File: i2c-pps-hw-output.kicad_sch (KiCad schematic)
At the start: 21 parts, among them J2 Vout, Q7 MMBT3904

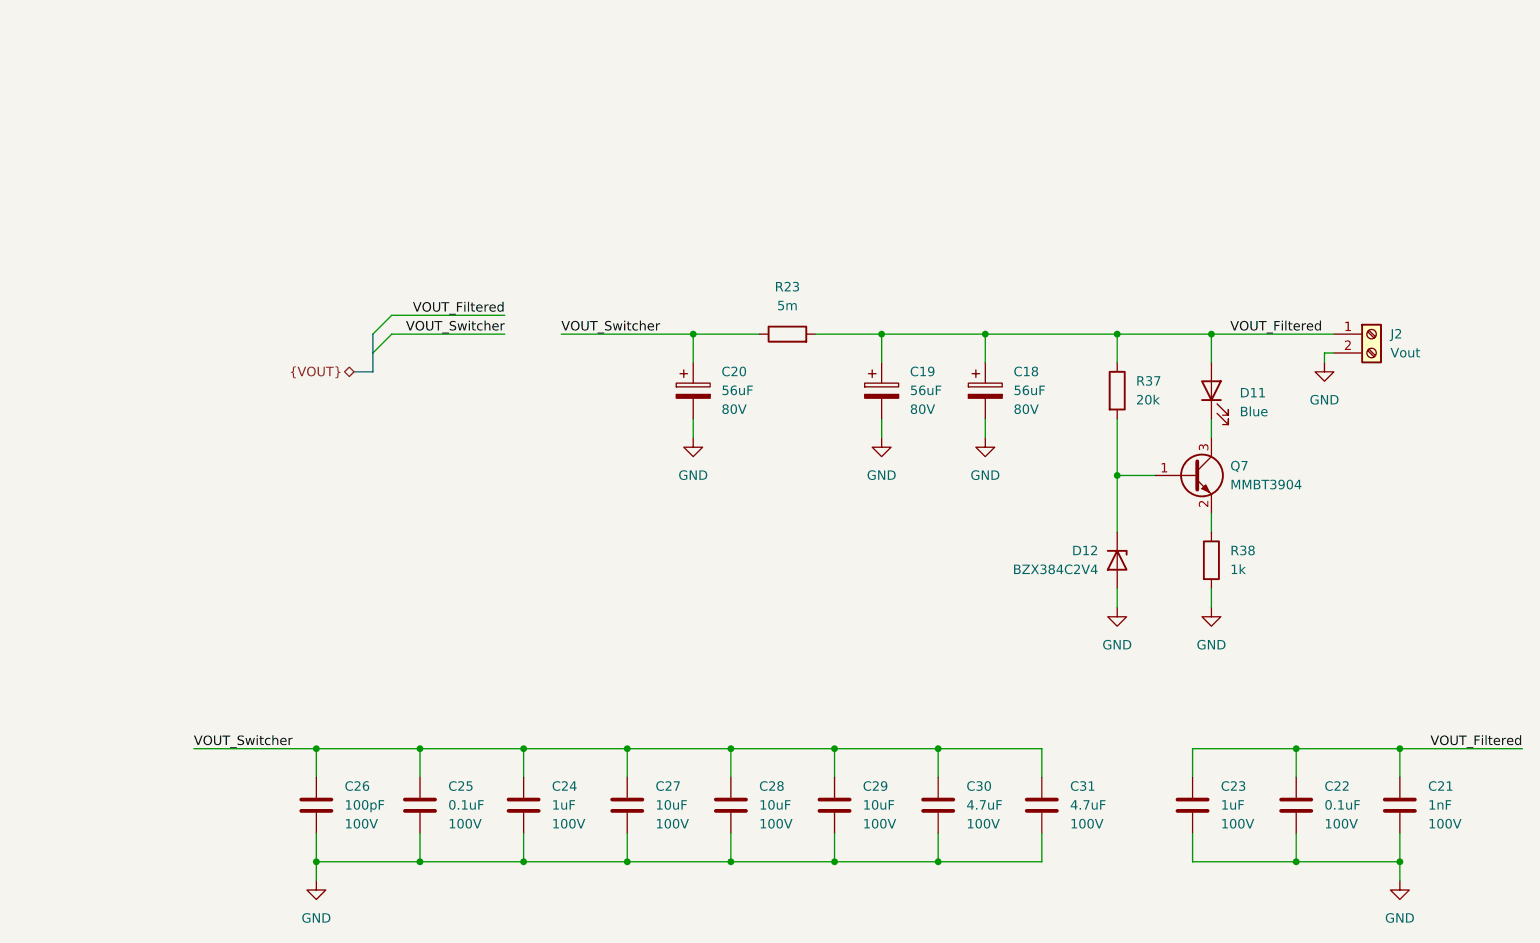
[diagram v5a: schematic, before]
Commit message: Route the PCB
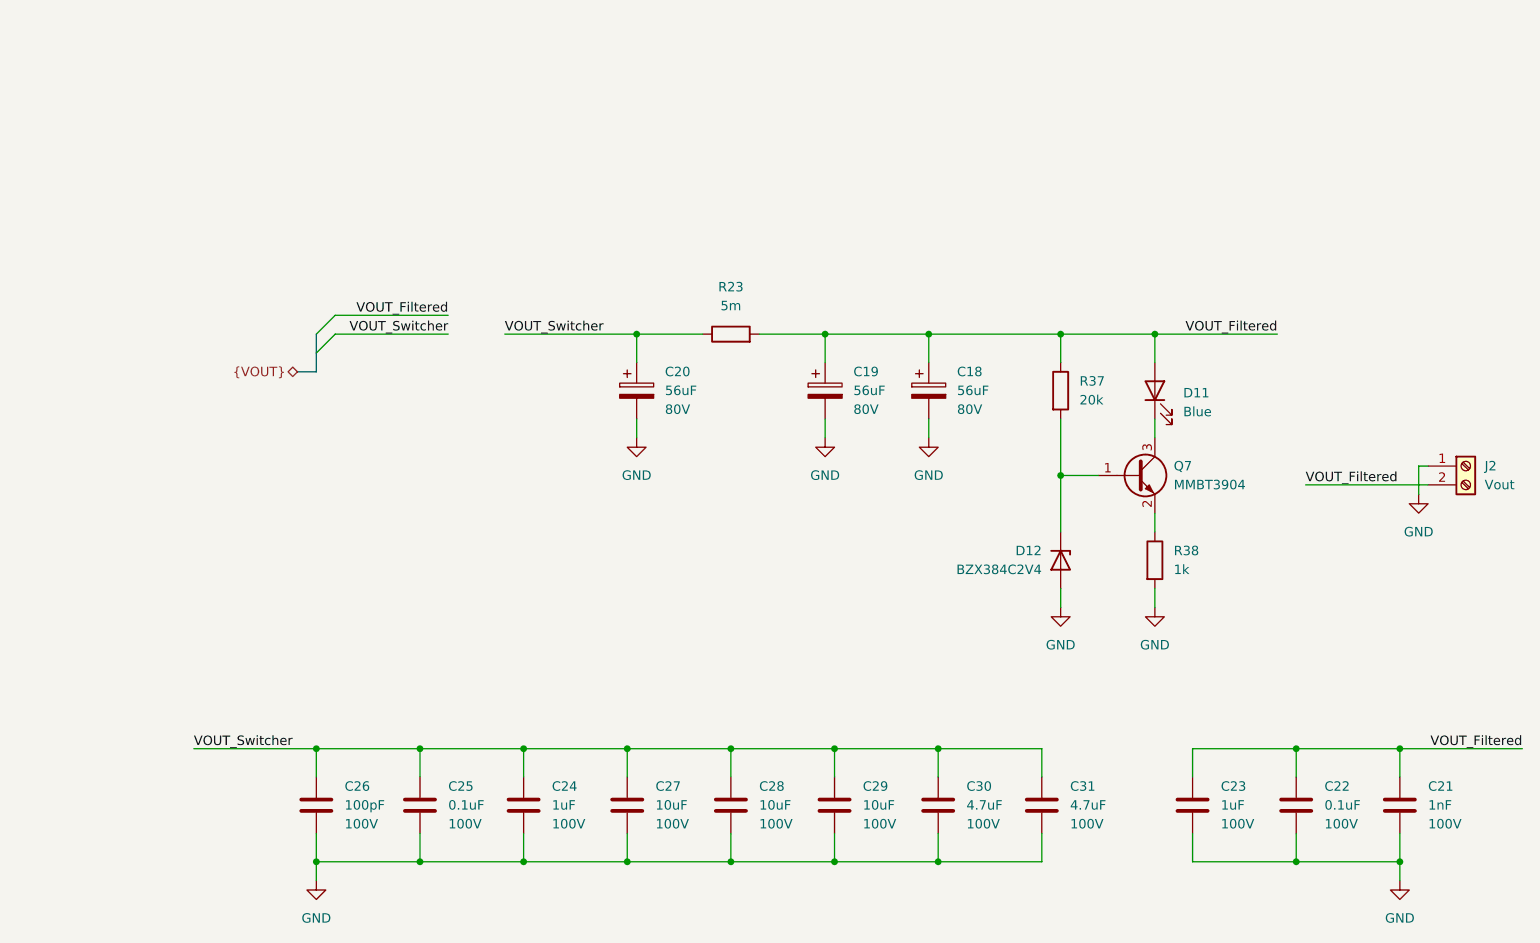
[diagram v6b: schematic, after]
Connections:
- net GND: now also J2.1 (Pin_1); no longer J2.2 (Pin_2)
- net VOUT_Filtered: now also J2.2 (Pin_2); no longer J2.1 (Pin_1)
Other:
- moved on the sheet: C18, C19, C20, D11, D12, J2, Q7, R23, R37, R38

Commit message: Add manufacturer and part number to Vout terminal
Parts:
- J2: Manufacturer (none) -> Same Sky (Formerly CUI Devices); Part Number (none) -> TB006-508-02BE
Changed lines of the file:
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@@
+			)
+		)
+		(property "Manufacturer" "Same Sky (Formerly CUI Devices)"
+			(at 220.98 83.82 0)
+			(effects
+				(font
+					(size 1.27 1.27)
+				)
+				(hide yes)
+			)
+		)
+		(property "Part Number" "TB006-508-02BE"
+			(at 220.98 83.82 0)
+			(effects
+				(font
+					(size 1.27 1.27)
+				)
+				(hide yes)
 			)
 		)
